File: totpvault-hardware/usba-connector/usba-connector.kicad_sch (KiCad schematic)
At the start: 29 parts, among them J3 Conn_01x06_Socket, U1 ESP32-C3, U2 HT75xx-1-SOT89, U3 CH343P, U4 USBLC6-2SC6, Y1 Crystal_GND24

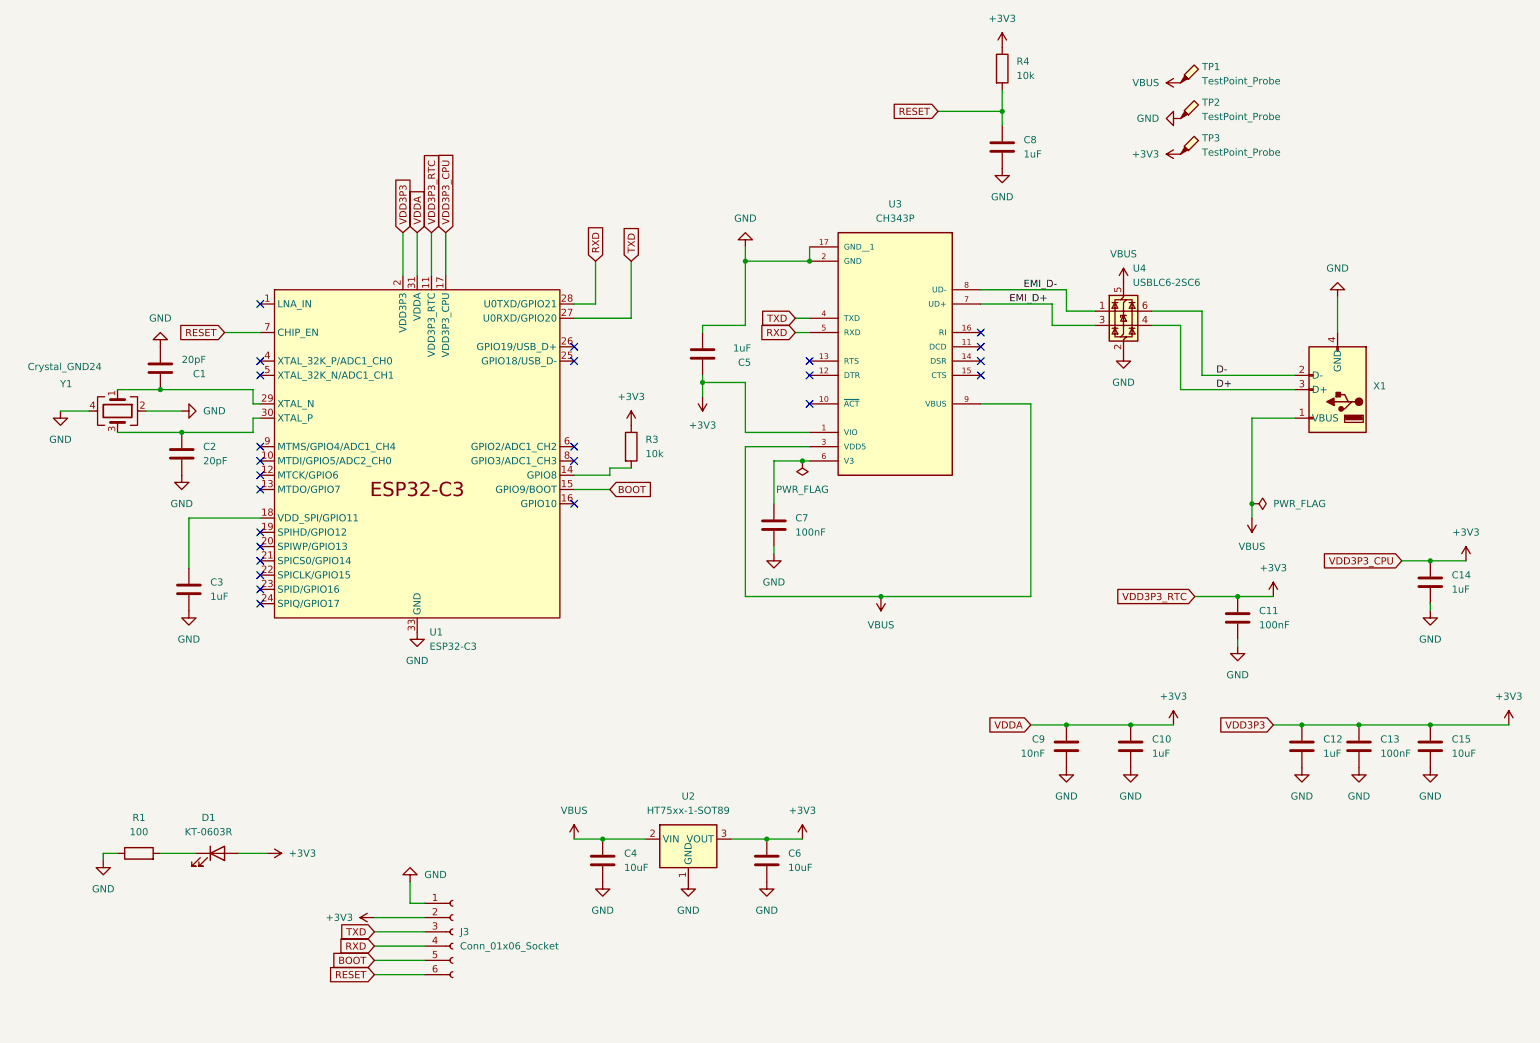
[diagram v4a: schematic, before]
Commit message: Finalized new board design with JLCPCB basic parts, code cleanup
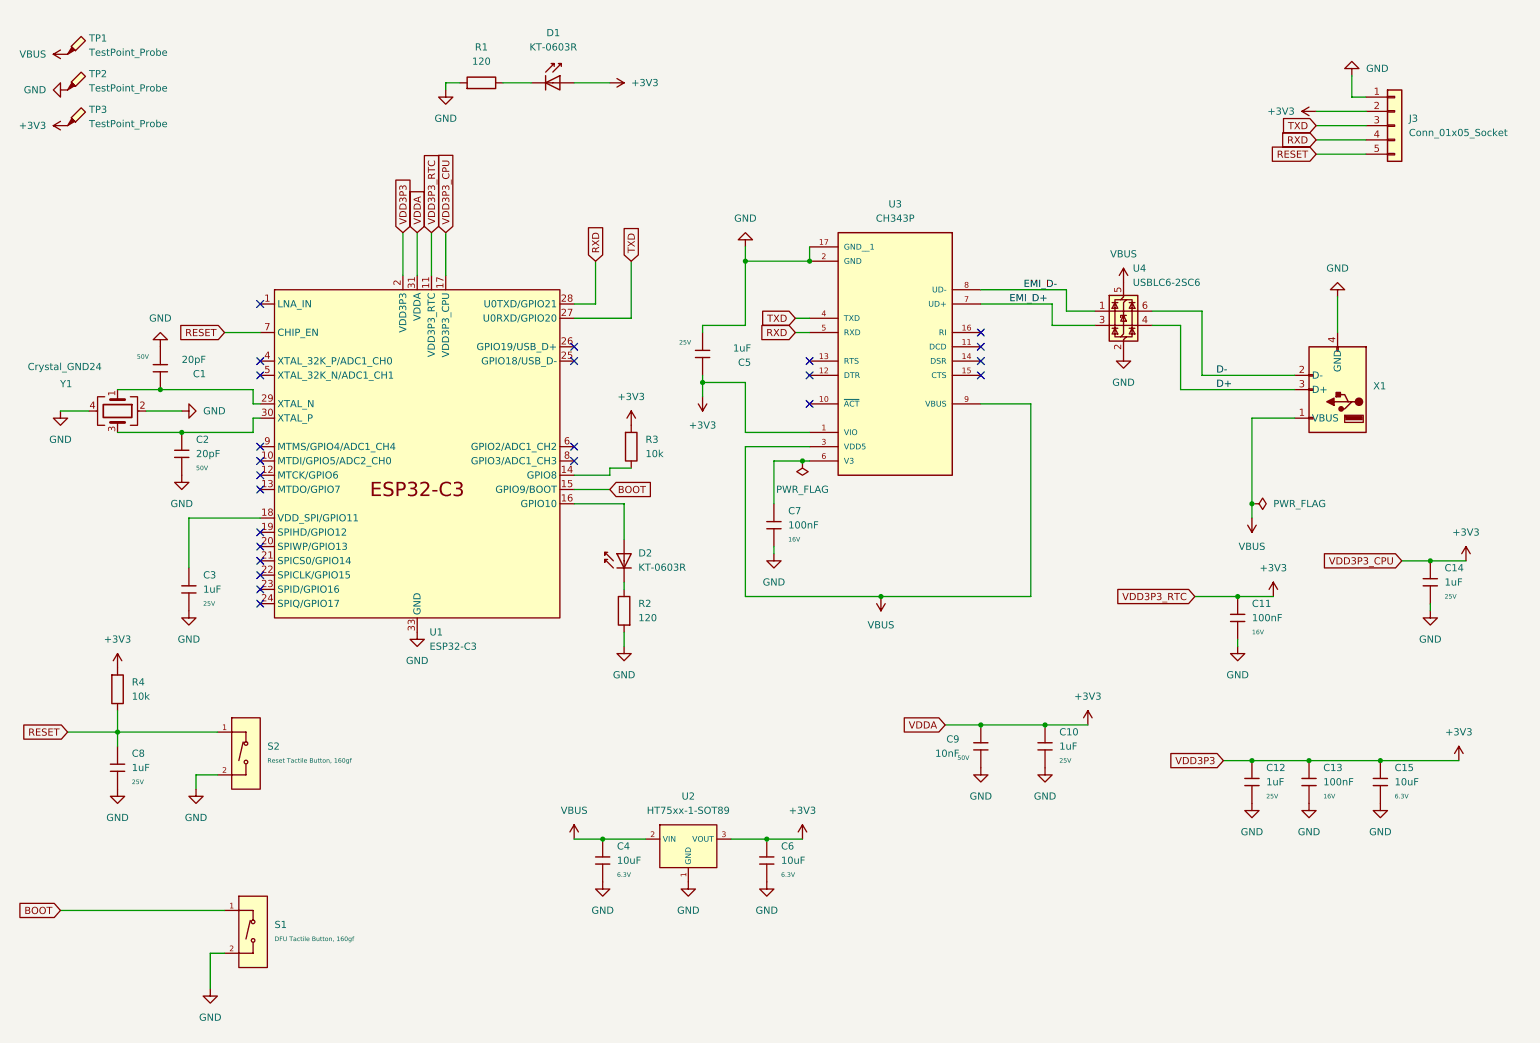
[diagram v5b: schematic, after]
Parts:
- added D2: KT-0603R, PCM_JLCPCB:D_0603, symbol PCM_JLCPCB-Diodes:LED,0603,Red
- added R2: 120, PCM_JLCPCB:R_0402, symbol PCM_JLCPCB-Resistors:0402,120Ω
- added S1: DFU Tactile Button, 160gf, PCM_JLCPCB:SW_TS-1088-AR02016, symbol PCM_JLCPCB-Connectors_Buttons:Tactile Button, 160gf, 12V, 50mA, 4.0mm
- added S2: Reset Tactile Button, 160gf, PCM_JLCPCB:SW_TS-1088-AR02016, symbol PCM_JLCPCB-Connectors_Buttons:Tactile Button, 160gf, 12V, 50mA, 4.0mm
- C1, C2: footprint Capacitor_SMD:C_0402_1005Metric -> PCM_JLCPCB:C_0402; symbol Device:C -> PCM_JLCPCB-Capacitors:0402,20pF; Attrition Qty (none) -> 10; Capacitance (none) -> 20pF; Category (none) -> Capacitors,Multilayer Ceramic Capacitors MLCC - SMD/SMT; Class (none) -> Basic Component; LCSC (none) -> C1554; Manufacturer (none) -> FH(Guangdong Fenghua Advanced Tech); Minimum Qty (none) -> 20; Part (none) -> 0402CG200J500NT; Price (none) -> 0.004USD; Process (none) -> SMT; Stock (none) -> 668698; Temperature Coefficient (none) -> C0G; Tolerance (none) -> ±5%; Voltage Rated (none) -> 50V
- C10, C12, C14, C3, C5, C8: footprint Capacitor_SMD:C_0402_1005Metric -> PCM_JLCPCB:C_0402; symbol Device:C -> PCM_JLCPCB-Capacitors:0402,1uF; Attrition Qty (none) -> 10; Capacitance (none) -> 1uF; Category (none) -> Capacitors,Multilayer Ceramic Capacitors MLCC - SMD/SMT; Class (none) -> Basic Component; LCSC (none) -> C52923; Manufacturer (none) -> Samsung Electro-Mechanics; Minimum Qty (none) -> 20; Part (none) -> CL05A105KA5NQNC; Price (none) -> 0.006USD; Process (none) -> SMT; Stock (none) -> 7021828; Temperature Coefficient (none) -> X5R; Tolerance (none) -> ±10%; Voltage Rated (none) -> 25V
- C11, C13, C7: footprint Capacitor_SMD:C_0402_1005Metric -> PCM_JLCPCB:C_0402; symbol Device:C -> PCM_JLCPCB-Capacitors:0402,100nF; Attrition Qty (none) -> 10; Capacitance (none) -> 100nF; Category (none) -> Capacitors,Multilayer Ceramic Capacitors MLCC - SMD/SMT; Class (none) -> Basic Component; LCSC (none) -> C1525; Manufacturer (none) -> Samsung Electro-Mechanics; Minimum Qty (none) -> 20; Part (none) -> CL05B104KO5NNNC; Price (none) -> 0.004USD; Process (none) -> SMT; Stock (none) -> 20208285; Temperature Coefficient (none) -> X7R; Tolerance (none) -> ±10%; Voltage Rated (none) -> 16V
- C15, C4, C6: footprint Capacitor_SMD:C_0402_1005Metric -> PCM_JLCPCB:C_0402; symbol Device:C -> PCM_JLCPCB-Capacitors:0402,10uF; Attrition Qty (none) -> 10; Capacitance (none) -> 10uF; Category (none) -> Capacitors,Multilayer Ceramic Capacitors MLCC - SMD/SMT; Class (none) -> Basic Component; LCSC (none) -> C15525; Manufacturer (none) -> Samsung Electro-Mechanics; Minimum Qty (none) -> 20; Part (none) -> CL05A106MQ5NUNC; Price (none) -> 0.009USD; Process (none) -> SMT; Stock (none) -> 3940889; Temperature Coefficient (none) -> X5R; Tolerance (none) -> ±20%; Voltage Rated (none) -> 6.3V
- C9: footprint Capacitor_SMD:C_0402_1005Metric -> PCM_JLCPCB:C_0402; symbol Device:C -> PCM_JLCPCB-Capacitors:0402,10nF; Attrition Qty (none) -> 10; Capacitance (none) -> 10nF; Category (none) -> Capacitors,Multilayer Ceramic Capacitors MLCC - SMD/SMT; Class (none) -> Basic Component; LCSC (none) -> C15195; Manufacturer (none) -> Samsung Electro-Mechanics; Minimum Qty (none) -> 20; Part (none) -> CL05B103KB5NNNC; Price (none) -> 0.005USD; Process (none) -> SMT; Stock (none) -> 4779042; Temperature Coefficient (none) -> X7R; Tolerance (none) -> ±10%; Voltage Rated (none) -> 50V
- D1: footprint LED_SMD:LED_0603_1608Metric -> PCM_JLCPCB:D_0603; symbol Device:LED -> PCM_JLCPCB-Diodes:LED,0603,Red; Attrition Qty (none) -> 10; Category (none) -> Optocouplers & LEDs & Infrared,Light Emitting Diodes (LED); Class (none) -> Basic Component; LCSC (none) -> C2286; Manufacturer (none) -> Hubei KENTO Elec; Minimum Qty (none) -> 20; Part (none) -> KT-0603R; Price (none) -> 0.009USD; Process (none) -> SMT; Stock (none) -> 5373336
- J3: value Conn_01x06_Socket -> Conn_01x05_Socket; footprint Connector_PinHeader_2.54mm:PinHeader_1x06_P2.54mm_Vertical -> Connector_PinHeader_2.54mm:PinHeader_1x05_P2.54mm_Vertical; symbol Connector:Conn_01x06_Socket -> Connector_Generic:Conn_01x05
- R1: value 100 -> 120; footprint Resistor_SMD:R_0402_1005Metric -> PCM_JLCPCB:R_0402; symbol Device:R -> PCM_JLCPCB-Resistors:0402,120Ω; Attrition Qty (none) -> 10; Category (none) -> Resistors,Chip Resistor - Surface Mount; Class (none) -> Basic Component; LCSC (none) -> C25079; Manufacturer (none) -> UNI-ROYAL(Uniroyal Elec); Minimum Qty (none) -> 20; Operating Temperature Range (none) -> -55°C~+155°C; Overload Voltage (Max) (none) -> 50V; Part (none) -> 0402WGF1200TCE; Power(Watts) (none) -> 62.5mW; Price (none) -> 0.004USD; Process (none) -> SMT; Resistance (none) -> 120Ω; Stock (none) -> 370600; Temperature Coefficient (none) -> ±100ppm/°C; Tolerance (none) -> ±1%; Type (none) -> Thick Film Resistors
- R3, R4: footprint Resistor_SMD:R_0402_1005Metric -> PCM_JLCPCB:R_0402; symbol Device:R -> PCM_JLCPCB-Resistors:0402,10kΩ; Attrition Qty (none) -> 10; Category (none) -> Resistors,Chip Resistor - Surface Mount; Class (none) -> Basic Component; LCSC (none) -> C25744; Manufacturer (none) -> UNI-ROYAL(Uniroyal Elec); Minimum Qty (none) -> 20; Operating Temperature Range (none) -> -55°C~+155°C; Overload Voltage (Max) (none) -> 50V; Part (none) -> 0402WGF1002TCE; Power(Watts) (none) -> 62.5mW; Price (none) -> 0.004USD; Process (none) -> SMT; Resistance (none) -> 10kΩ; Stock (none) -> 24372091; Temperature Coefficient (none) -> ±100ppm/°C; Tolerance (none) -> ±1%; Type (none) -> Thick Film Resistors
- U2: footprint Package_TO_SOT_SMD:SOT-89-3 -> PCM_JLCPCB:SOT-89-3_L4.5-W2.5-P1.50-LS4.2-BR; symbol Regulator_Linear:HT75xx-1-SOT89 -> PCM_JLCPCB-Power:LDO, 3.3V, 0.1A; Attrition Qty (none) -> 2; Category (none) -> Power Management ICs,Linear Voltage Regulators (LDO); Class (none) -> Basic Component; Dropout Voltage (none) -> 55mV@(1mA); LCSC (none) -> C14289; Manufacturer (none) -> Holtek Semicon; Maximum Input Voltage (none) -> 30V; Minimum Qty (none) -> 5; Number Of Outputs (none) -> 1; Output Current (none) -> 100mA; Output Polarity (none) -> Positive electrode; Output Type (none) -> Fixed; Output Voltage (none) -> 3.3V; Part (none) -> HT7533-1; Price (none) -> 0.113USD; Process (none) -> SMT; Stock (none) -> 103659
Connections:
- net BOOT: now also S1.1 (A); no longer J3.5 (Pin_5)
- net GND: now also R2.1, S1.2 (B), S2.2 (B)
- net RESET: now also J3.5 (Pin_5), S2.1 (A); no longer J3.6 (Pin_6)
- net at U1.16 (GPIO10): now also D2.2
- new net: D2.1, R2.2
- no-connect marks 25 -> 24
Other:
- moved on the sheet: C10, C12, C13, C15, C8, C9, R1, R4, TP1, TP2, TP3

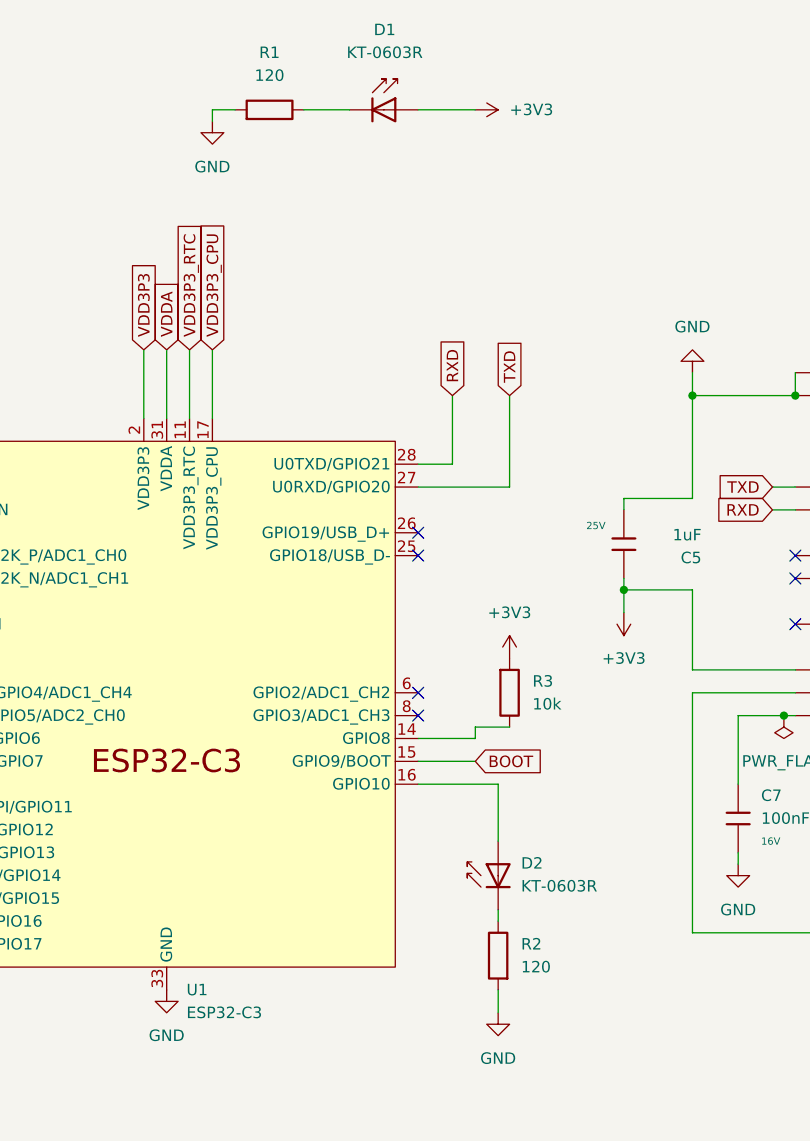
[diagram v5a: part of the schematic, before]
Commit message: Updated documentation with schematics and images, delete GUI project, PCB 3D design cleanup
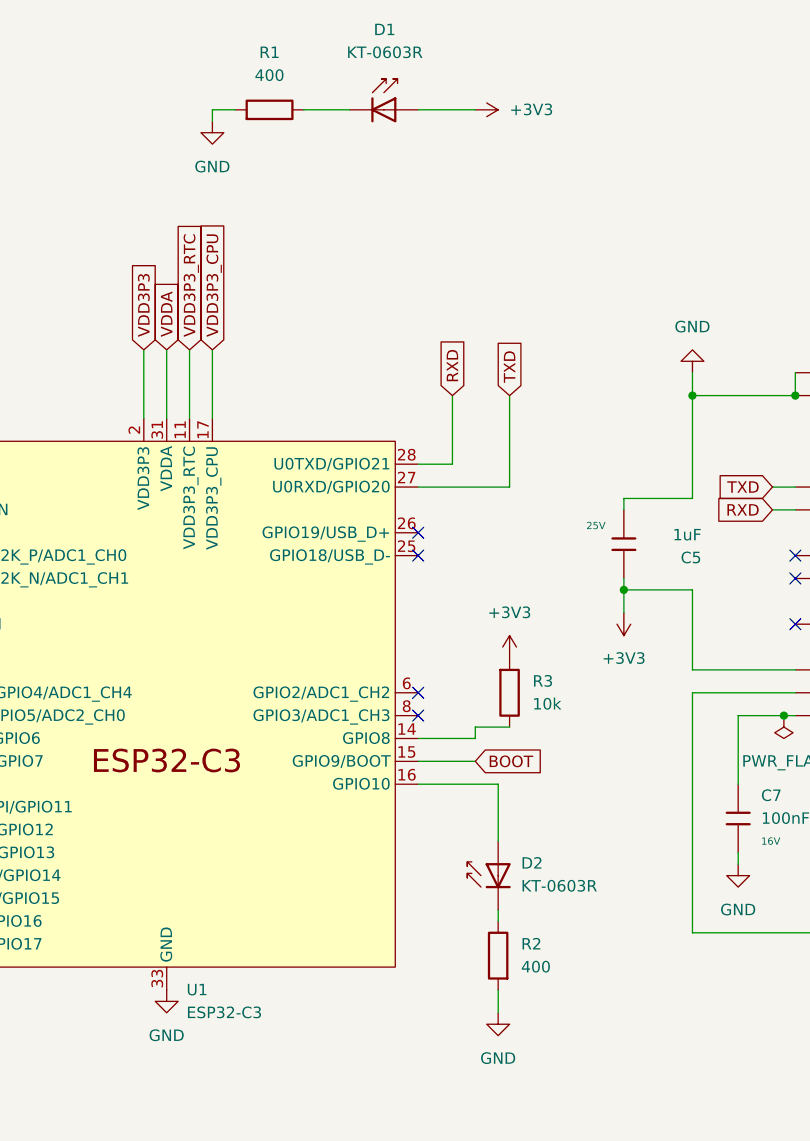
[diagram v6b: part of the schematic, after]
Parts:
- R1, R2: value 120 -> 400
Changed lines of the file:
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@@
 			)
 		)
-		(property "Value" "120"
+		(property "Value" "400"
 			(at 99.06 21.59 90)
 			(effects
@@
 			)
 		)
-		(property "Value" "120"
+		(property "Value" "400"
 			(at 127 120.6499 0)
 			(effects
